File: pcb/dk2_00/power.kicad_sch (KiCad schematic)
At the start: 12 parts, among them J15 Conn_02x05_Odd_Even, J16 Barrel_Jack_Switch, U12 XL1509-5.0, U13 L7805

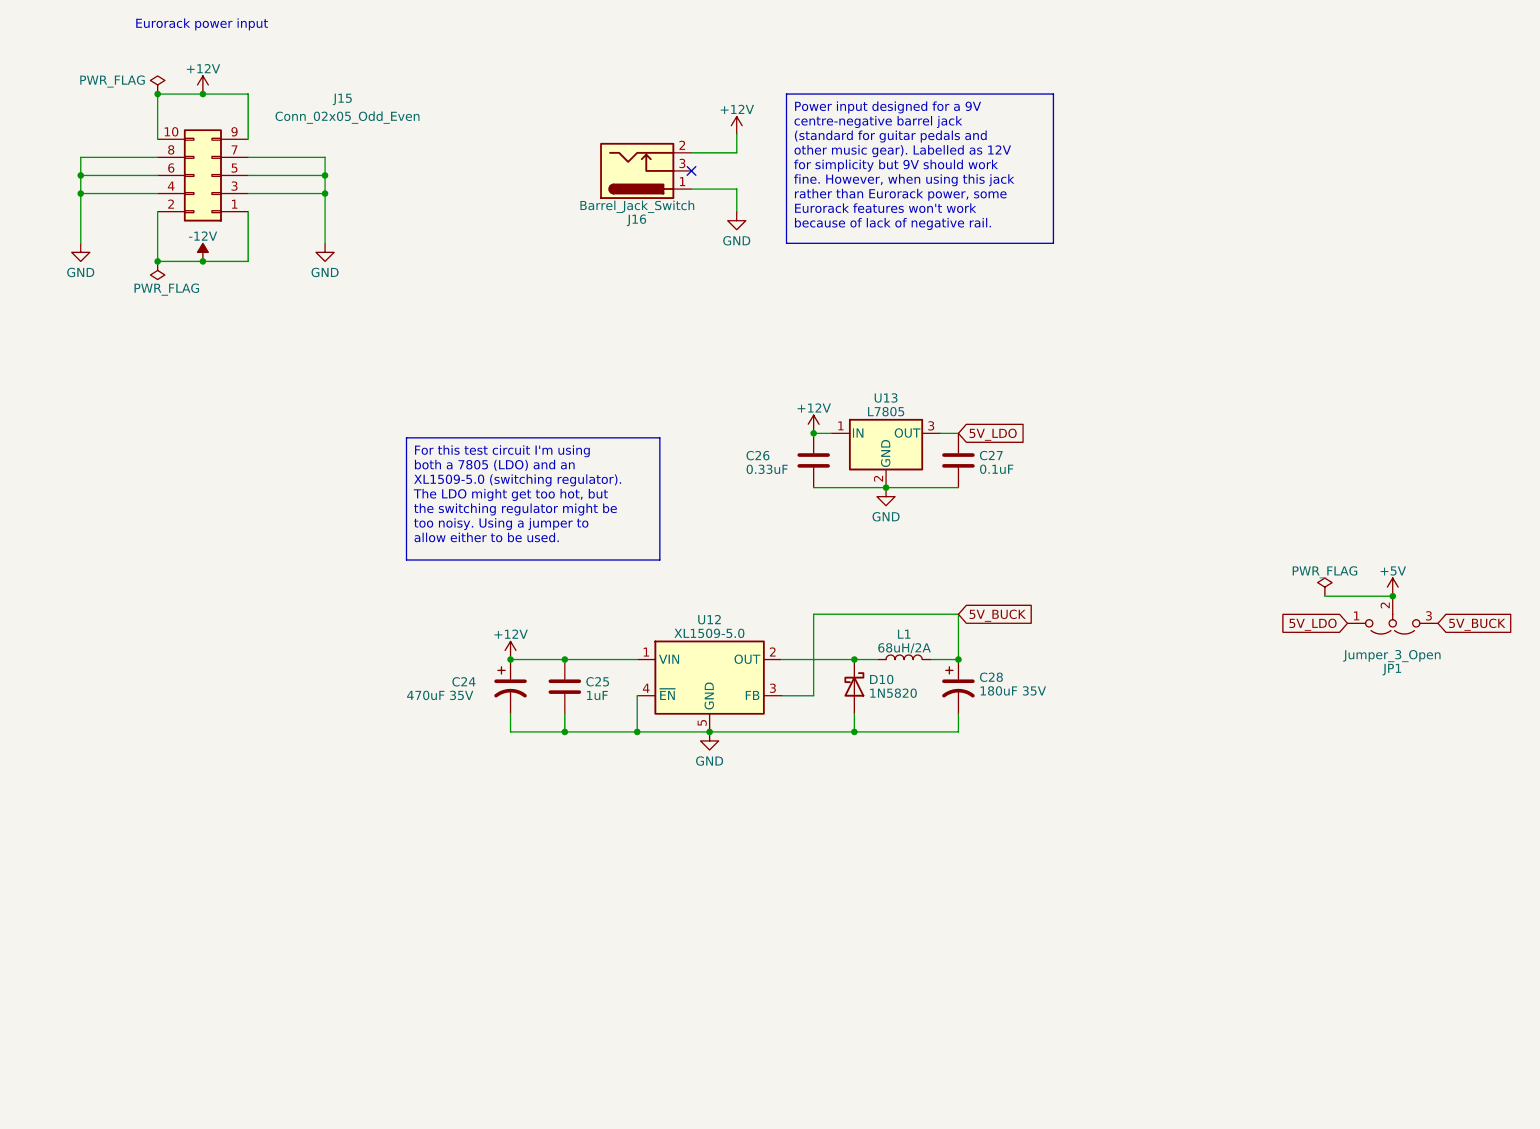
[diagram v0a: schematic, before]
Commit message: barrel jack, power pins
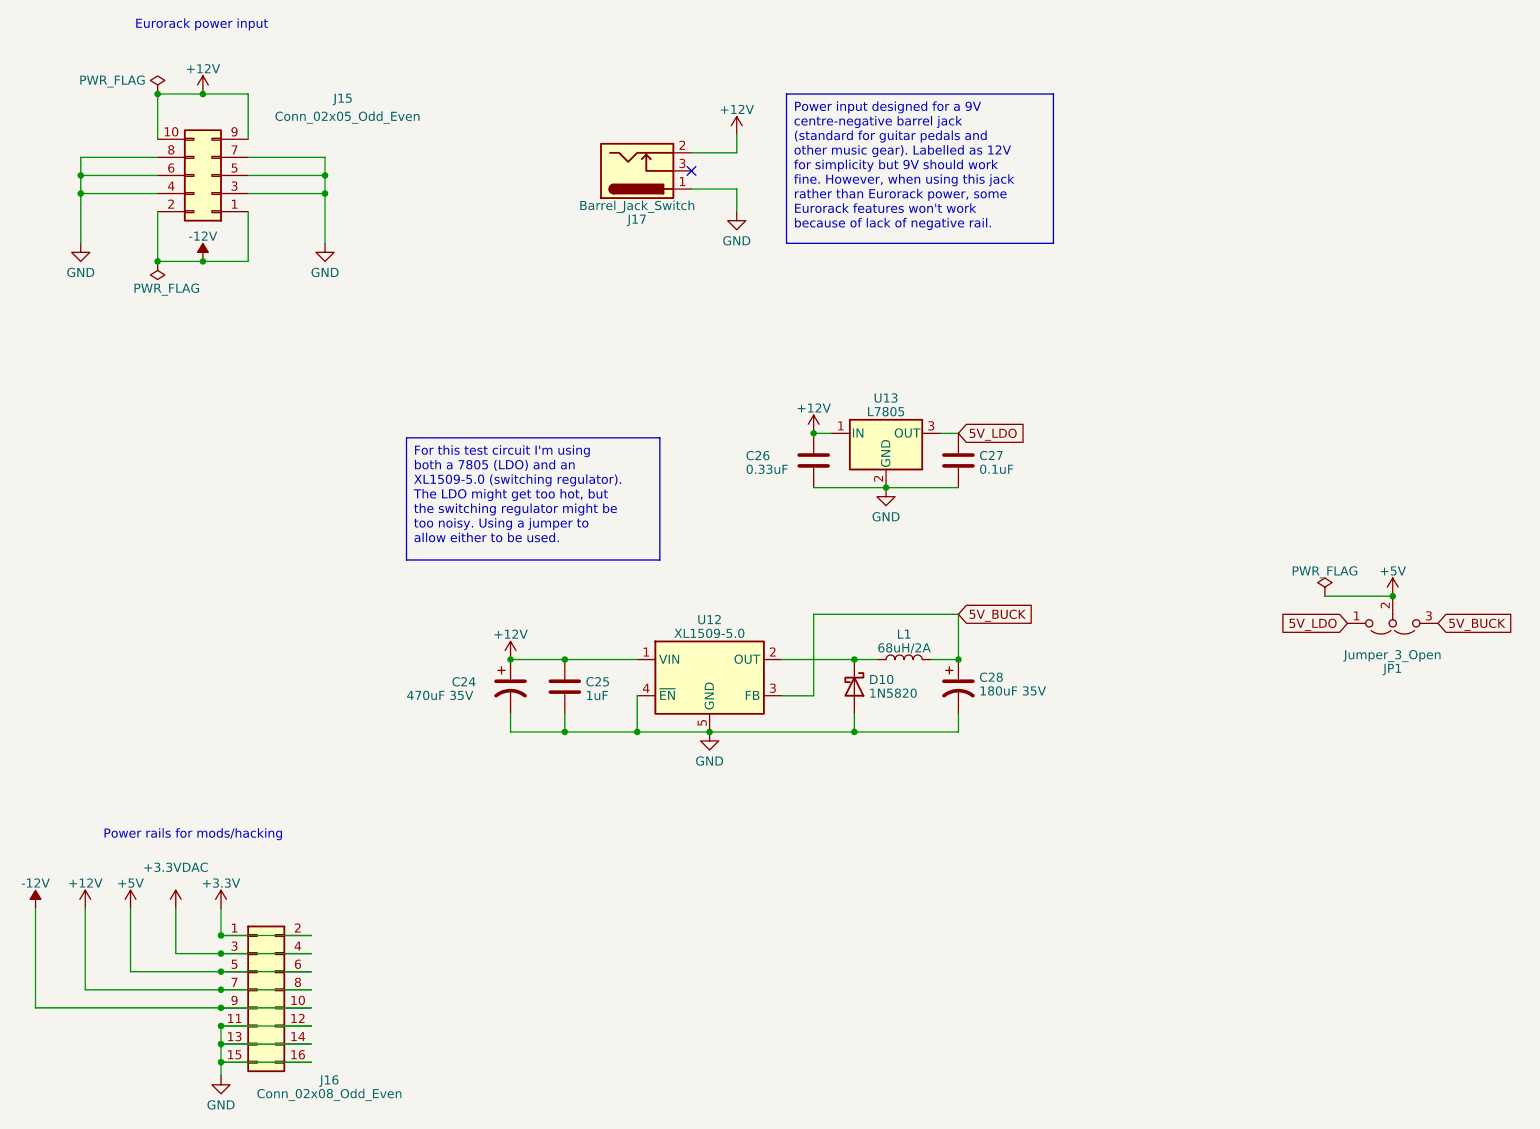
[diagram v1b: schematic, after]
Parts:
- added J16: Conn_02x08_Odd_Even, symbol Connector_Generic:Conn_02x08_Odd_Even
- renumbered J16 to J17
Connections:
- net +12V: now also J16.7 (Pin_7), J16.8 (Pin_8)
- net +5V: now also J16.5 (Pin_5), J16.6 (Pin_6)
- net -12V: now also J16.10 (Pin_10), J16.9 (Pin_9)
- net GND: now also J16.11 (Pin_11), J16.12 (Pin_12), J16.13 (Pin_13), J16.14 (Pin_14), J16.15 (Pin_15), J16.16 (Pin_16)
- new net +3.3V: J16.1 (Pin_1), J16.2 (Pin_2)
- new net +3.3VDAC: J16.3 (Pin_3), J16.4 (Pin_4)
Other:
- note added: "Power rails for mods/hacking"

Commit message: components...
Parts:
- C24, C28: footprint (none) -> Capacitor_THT:CP_Radial_D10.0mm_P5.00mm
- C25, C26, C27: footprint (none) -> Capacitor_SMD:C_0603_1608Metric
- J15: footprint (none) -> Connector_PinHeader_2.54mm:PinHeader_2x05_P2.54mm_Vertical
- J16: footprint (none) -> Connector_PinHeader_2.54mm:PinHeader_2x08_P2.54mm_Vertical
- J17: footprint (none) -> Connector_BarrelJack:BarrelJack_Horizontal
- JP1: footprint (none) -> Connector_PinHeader_2.54mm:PinHeader_1x03_P2.54mm_Vertical
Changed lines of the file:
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@@
       (effects (font (size 1.27 1.27)) (justify left))
     )
-    (property "Footprint" "" (at 104.775 117.475 0)
+    (property "Footprint" "Capacitor_THT:CP_Radial_D10.0mm_P5.00mm" (at 104.775 117.475 0)
       (effects (font (size 1.27 1.27)) hide)
     )
@@
       (effects (font (size 1.27 1.27)) (justify left))
     )
-    (property "Footprint" "" (at 113.3602 121.285 0)
+    (property "Footprint" "Capacitor_SMD:C_0603_1608Metric" (at 113.3602 121.285 0)
       (effects (font (size 1.27 1.27)) hide)
     )
@@
       (effects (font (size 1.27 1.27)) (justify left))
     )
-    (property "Footprint" "" (at 168.6052 89.535 0)
+    (property "Footprint" "Capacitor_SMD:C_0603_1608Metric" (at 168.6052 89.535 0)
       (effects (font (size 1.27 1.27)) hide)
     )
@@
       (effects (font (size 1.27 1.27)))
     )
-    (property "Footprint" "" (at 69.215 160.02 0)
+    (property "Footprint" "Connector_PinHeader_2.54mm:PinHeader_2x08_P2.54mm_Vertical" (at 69.215 160.02 0)
       (effects (font (size 1.27 1.27)) hide)
     )
@@
       (effects (font (size 1.27 1.27)))
     )
-    (property "Footprint" "" (at 62.865 45.72 0)
+    (property "Footprint" "Connector_PinHeader_2.54mm:PinHeader_2x05_P2.54mm_Vertical" (at 62.865 45.72 0)
       (effects (font (size 1.27 1.27)) hide)
     )
@@
       (effects (font (size 1.27 1.27)))
     )
-    (property "Footprint" "" (at 123.825 44.069 0)
+    (property "Footprint" "Connector_BarrelJack:BarrelJack_Horizontal" (at 123.825 44.069 0)
       (effects (font (size 1.27 1.27)) hide)
     )
@@
       (effects (font (size 1.27 1.27)))
     )
-    (property "Footprint" "" (at 228.6 108.585 0)
+    (property "Footprint" "Connector_PinHeader_2.54mm:PinHeader_1x03_P2.54mm_Vertical" (at 228.6 108.585 0)
       (effects (font (size 1.27 1.27)) hide)
     )
@@
       (effects (font (size 1.27 1.27)) (justify left))
     )
-    (property "Footprint" "" (at 148.2852 89.535 0)
+    (property "Footprint" "Capacitor_SMD:C_0603_1608Metric" (at 148.2852 89.535 0)
       (effects (font (size 1.27 1.27)) hide)
     )
@@
       (effects (font (size 1.27 1.27)) (justify left))
     )
-    (property "Footprint" "" (at 167.64 117.475 0)
-      (effects (font (size 1.27 1.27)) hide)
-    )
+    (property "Footprint" "Capacitor_THT:CP_Radial_D10.0mm_P5.00mm" (at 167.64 117.475 0)
+      (effects (font (size 1.27 1.27)) hide)
+    )

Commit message: footprints assigned
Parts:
- L1: footprint (none) -> Inductor_THT:L_Radial_D8.7mm_P5.00mm_Fastron_07HCP
- U13: footprint (none) -> Package_TO_SOT_SMD:TO-252-2
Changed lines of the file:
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@@
       (effects (font (size 1.27 1.27)))
     )
-    (property "Footprint" "" (at 160.02 113.665 0)
+    (property "Footprint" "Inductor_THT:L_Radial_D8.7mm_P5.00mm_Fastron_07HCP" (at 160.02 113.665 0)
       (effects (font (size 1.27 1.27)) hide)
     )
@@
       (effects (font (size 1.27 1.27)))
     )
-    (property "Footprint" "" (at 158.115 85.725 0)
+    (property "Footprint" "Package_TO_SOT_SMD:TO-252-2" (at 158.115 85.725 0)
       (effects (font (size 1.27 1.27) italic) (justify left) hide)
     )

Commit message: this layout is complicated!
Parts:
- J15: value Conn_02x05_Odd_Even -> Eurorack_Power
- J16: value Conn_02x08_Odd_Even -> Power_Breakout
- J17: value Barrel_Jack_Switch -> 9V_Power_Input
- JP1: value Jumper_3_Open -> 5V_Jumper
- renumbered C24 to C25, C25 to C26, C26 to C27, C27 to C28, C28 to C29
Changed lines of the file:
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@@
   (symbol (lib_id "Device:C_Polarized_US") (at 104.775 117.475 0) (unit 1)
     (in_bom yes) (on_board yes) (dnp no)
-    (property "Reference" "C24" (at 96.52 116.84 0)
+    (property "Reference" "C25" (at 96.52 116.84 0)
       (effects (font (size 1.27 1.27)) (justify left))
     )
@@
       (project "dk2_00"
         (path "/87a59a99-d509-467e-85da-26d34072acb7/be1ddc4d-f499-4b75-b4b5-b626a320d90d"
-          (reference "C24") (unit 1)
+          (reference "C25") (unit 1)
         )
       )
@@
   (symbol (lib_id "Device:C") (at 112.395 117.475 0) (unit 1)
     (in_bom yes) (on_board yes) (dnp no) (fields_autoplaced)
-    (property "Reference" "C25" (at 115.316 116.8313 0)
+    (property "Reference" "C26" (at 115.316 116.8313 0)
       (effects (font (size 1.27 1.27)) (justify left))
     )
@@
       (project "dk2_00"
         (path "/87a59a99-d509-467e-85da-26d34072acb7/be1ddc4d-f499-4b75-b4b5-b626a320d90d"
-          (reference "C25") (unit 1)
+          (reference "C26") (unit 1)
         )
       )
@@
   (symbol (lib_id "Device:C") (at 167.64 85.725 0) (unit 1)
     (in_bom yes) (on_board yes) (dnp no) (fields_autoplaced)
-    (property "Reference" "C27" (at 170.561 85.0813 0)
+    (property "Reference" "C28" (at 170.561 85.0813 0)
       (effects (font (size 1.27 1.27)) (justify left))
     )
@@
       (project "dk2_00"
         (path "/87a59a99-d509-467e-85da-26d34072acb7/be1ddc4d-f499-4b75-b4b5-b626a320d90d"
-          (reference "C27") (unit 1)
+          (reference "C28") (unit 1)
         )
       )
@@
       (effects (font (size 1.27 1.27)))
     )
-    (property "Value" "Conn_02x08_Odd_Even" (at 79.375 174.641 0)
+    (property "Value" "Power_Breakout" (at 79.375 174.641 0)
       (effects (font (size 1.27 1.27)))
     )
@@
       (effects (font (size 1.27 1.27)))
     )
-    (property "Value" "Conn_02x05_Odd_Even" (at 81.915 37.465 0)
+    (property "Value" "Eurorack_Power" (at 81.915 37.465 0)
       (effects (font (size 1.27 1.27)))
     )
@@
       (effects (font (size 1.27 1.27)))
     )
-    (property "Value" "Barrel_Jack_Switch" (at 122.555 49.9839 0)
+    (property "Value" "9V_Power_Input" (at 122.555 49.9839 0)
       (effects (font (size 1.27 1.27)))
     )
@@
       (effects (font (size 1.27 1.27)))
     )
-    (property "Value" "Jumper_3_Open" (at 228.6 113.03 0)
+    (property "Value" "5V_Jumper" (at 228.6 113.03 0)
       (effects (font (size 1.27 1.27)))
     )
@@
   (symbol (lib_id "Device:C") (at 147.32 85.725 0) (unit 1)
     (in_bom yes) (on_board yes) (dnp no)
-    (property "Reference" "C26" (at 137.795 85.09 0)
+    (property "Reference" "C27" (at 137.795 85.09 0)
       (effects (font (size 1.27 1.27)) (justify left))
     )
@@
       (project "dk2_00"
         (path "/87a59a99-d509-467e-85da-26d34072acb7/be1ddc4d-f499-4b75-b4b5-b626a320d90d"
-          (reference "C26") (unit 1)
+          (reference "C27") (unit 1)
         )
       )
@@
   (symbol (lib_id "Device:C_Polarized_US") (at 167.64 117.475 0) (unit 1)
     (in_bom yes) (on_board yes) (dnp no) (fields_autoplaced)
-    (property "Reference" "C28" (at 170.561 116.1963 0)
+    (property "Reference" "C29" (at 170.561 116.1963 0)
       (effects (font (size 1.27 1.27)) (justify left))
     )
@@
       (project "dk2_00"
         (path "/87a59a99-d509-467e-85da-26d34072acb7/be1ddc4d-f499-4b75-b4b5-b626a320d90d"
-          (reference "C28") (unit 1)
-        )
-      )
+          (reference "C29") (unit 1)
+        )
+      )
